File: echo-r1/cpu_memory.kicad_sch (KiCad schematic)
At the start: 48 parts, among them U6 STM32H743IGTx, U7 W9825G6KH-x, Y1 SC-32S32.768kHz20PPM12.5pF, Y2 XTM32024000JT00351001

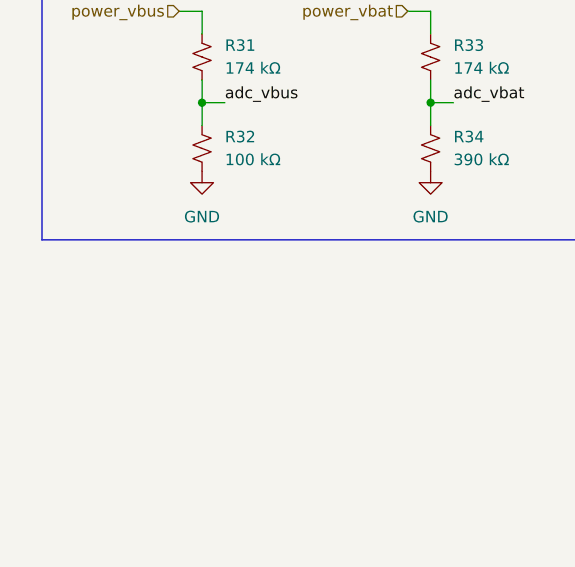
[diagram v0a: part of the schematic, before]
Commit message: R1-Rev1: remove VBUS discharge resistor
This is not needed since there is a path through the ADC
voltage divider to discharge VBUS -- and realistically
the battery charger should also discharge VBUS even with
no resistive path to ground.
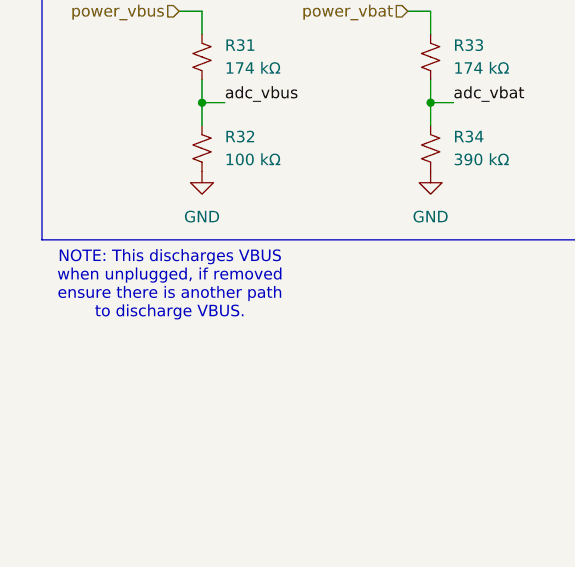
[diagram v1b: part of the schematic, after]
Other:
- note added: "NOTE: This discharges VBUS when unplugged, if removed ensure there is another path to discharge VBUS."
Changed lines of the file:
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@@
+		)
+	)
+	(text "NOTE: This discharges VBUS\nwhen unplugged, if removed\nensure there is another path\nto discharge VBUS."
+		(exclude_from_sim no)
+		(at 29.464 152.4 0)
+		(effects
+			(font
+				(size 1.27 1.27)
+			)
 		)
 	)

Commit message: WIP redesign with STM32H7R3Z8J6
The H7R3 has a bunch of features that greatly simplify the design:
support for HyperRAM, which requires far fewer pins than SDRAM and
is more power efficient; this frees up the FMC to interface with the
display in 8-bit 8080 MCU mode; and there is a built-in USB HS PHY,
removing the need for an external PHY.

The huge reduction in signal count allows for a smaller pin count
package -- only 144 pins. HyperRAM only comes in BGA packages so it
makes sense to also use the UFBGA-144 package for the CPU, which
takes up less than 1/4 of the board area of an LQFP-176 package.
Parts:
- removed C10, C11, C13, C14, C15, C16, C17, C18, C19, C21, C22, C23, C24, C25, C26, C32, C35, C36, C37, C38, C39, C40, C41, C9: 100 nF, Capacitor_SMD:C_0402_1005Metric, symbol Device:C_Small
- removed C12, C20: 1 µF, Capacitor_SMD:C_0402_1005Metric, symbol Device:C_Small
- removed C29: 4.7 µF, Capacitor_SMD:C_0603_1608Metric, symbol Device:C_Small
- removed C33, C34: 2.2 µF, Capacitor_SMD:C_0603_1608Metric, symbol Device:C_Small
- removed R10: 100 kΩ, Resistor_SMD:R_0402_1005Metric, symbol Device:R_Small_US
- removed R11, R12: 10 kΩ, Resistor_SMD:R_0402_1005Metric, symbol Device:R_Small_US
- removed U6: STM32H743IGTx, Package_QFP:LQFP-176_24x24mm_P0.5mm, symbol MCU_ST_STM32H7:STM32H743IGTx
- removed U7: W9825G6KH-x, Package_SO:TSOP-II-54_22.2x10.16mm_P0.8mm, symbol echoplayer:W9825G6KH-5
- added R23, R24: 10 kΩ, Resistor_SMD:R_0603_1608Metric_Pad0.98x0.95mm_HandSolder, symbol Device:R_US
- added U7: STM32H7R3Z8Jx, Package_BGA:UFBGA-144_10x10mm_Layout12x12_P0.8mm, symbol MCU_ST_STM32H7:STM32H7R3Z8Jx
- added U8: W958D8NBYA5I, echoplayer:TFBGA-24_6x8mm_Layout5x5_P1.0mm_Ball0.4mm, symbol echoplayer:W958D8NBYA5I
- renumbered C28 to C10, C30 to C11, C31 to C12, C27 to C9, D12 to D1, D13 to D2, D14 to D3, D15 to D4, R31 to R10, R32 to R11, R33 to R12, R34 to R13
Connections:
- net GND: now also U7.A1 (VSS), U7.A12 (VSS), U7.C9 (VSS), U7.D2 (VSS), U7.D5 (VSS), U7.D7 (VSS), U7.D8 (VSSUSB), U7.E1 (VSSSMPS), U7.E7 (VSS), U7.F5 (VSS), U7.G1 (VSS), U7.G8 (VSS), U7.H3 (VSSA), U7.H4 (VSS), U7.H7 (VSS), U7.K10 (VSS), U7.K6 (VSS), U7.K8 (VSS), U7.M1 (VSS), U7.M12 (VSS), U8.B3 (VSS), U8.C1 (VSSQ), U8.E5 (VSSQ)
- net codec.bclk: now also U7.D1 (PE5)
- net codec.dplay: now also U7.E2 (PE6)
- net codec.drec: now also U7.D3 (PE3)
- net codec.mclk: now also U7.C4 (PE2)
- net codec.wclk: now also U7.E3 (PE4)
- net codec_ctl.scl: now also R24.2, U7.A2 (PB8)
- net codec_ctl.sda: now also R23.2, U7.D4 (PB7)
- net osc24m_in: now also U7.G2 (PH0)
- net osc24m_out: now also U7.H1 (PH1)
- net osc32k_in: now also U7.C1 (PC14)
- net osc32k_out: now also U7.C2 (PC15)
- net power_3v3: now also R23.1, R24.1
- net rtc_wakeup: now also U7.B2 (PC13)
- net sdmmc.clk: now also U7.C12 (PC12)
- net sdmmc.cmd: now also U7.C11 (PD2)
- net sdmmc.d0: now also U7.G11 (PC8)
- net sdmmc.d1: now also U7.G10 (PC9)
- net sdmmc.d2: now also U7.D11 (PC10)
- net sdmmc.d3: now also U7.E9 (PC11)
- net swd_clk: now also U7.E10 (PA14(JTCK)
- net swd_io: now also U7.E12 (PA13(JTMS)
- net swd_nrst: now also U7.F4 (NRST)
- net power_vbus renamed usb_vbus
- net usb_vbus: now also U7.B8 (PM8)
- new net: U8.A5 (RFU), U8.B5 (RFU), U8.C2 (RFU), U8.C5 (RFU)
- new net lcd_mcu.cs: U7.K11 (PD12)
- new net lcd_mcu.d0: U7.E11 (PA12)
- new net lcd_mcu.d1: U7.F12 (PA11)
- new net lcd_mcu.d2: U7.F11 (PA10)
- new net lcd_mcu.d3: U7.G12 (PA9)
- new net lcd_mcu.d4: U7.F10 (PA8)
- new net lcd_mcu.d5: U7.L1 (PA2)
- new net lcd_mcu.d6: U7.J2 (PA1)
- new net lcd_mcu.d7: U7.K1 (PA0)
- new net lcd_mcu.dcx: U7.G5 (PC1)
- new net lcd_mcu.wrx: U7.L5 (PB2)
- new net power_1v8: U7.K5 (VDDXSPI1), U7.K7 (VDDXSPI1), U7.K9 (VDDXSPI1), U8.B4 (VCC), U8.D1 (VCCQ), U8.E4 (VCCQ)
- new net usb_d+: U7.A9 (PM6)
- new net usb_d-: U7.B9 (PM5)
- new net xspi_ck+: U7.M7 (PO4), U8.B2 (CK)
- new net xspi_ck-: U7.L7 (PO5), U8.A2 (CK#)
- new net xspi_cs: U7.J7 (PO0), U8.A3 (CS#)
- new net xspi_d0: U7.L8 (PP0), U8.D3 (DQ0)
- new net xspi_d1: U7.L10 (PP1), U8.D2 (DQ1)
- new net xspi_d2: U7.L6 (PP2), U8.C4 (DQ2)
- new net xspi_d3: U7.M6 (PP3), U8.D4 (DQ3)
- new net xspi_d4: U7.M5 (PP4), U8.D5 (DQ4)
- new net xspi_d5: U7.M8 (PP5), U8.E3 (DQ5)
- new net xspi_d6: U7.M9 (PP6), U8.E2 (DQ6)
- new net xspi_d7: U7.M10 (PP7), U8.E1 (DQ7)
- new net xspi_dqs0: U7.L9 (PO2), U8.C3 (RWDS)
- no-connect marks 8 -> 0
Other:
- note removed: "Any W9825G6KH variant"
- note removed: "BOOT0 must be high to force DFU mode. The STM32H743 has the 'old' ST boot pin structure which requires an external pulldown and cannot be used as a GPIO."
- note removed: "NOTE: As per errata 2.2.28, PC13 toggling can affect the LSE oscillator on LQFP. This is probably not a huge issue if the pin doesn't toggle very frequently, as is the case for RTC wakeup."
- note removed: "Note that the LCD bus connection is MSB to MSB, so in general STM32's LCD_X(n) -> lcd.x(n-2) since the STM32 has an 8 bit per channel LCD controller"
- note removed: "Or STM32H743IIT"
- note removed: "SDRAM"
- note removed: "SDRAM DECOUPLING Place 1x near VDD/VDDQ"
- note removed: "VDD DECOUPLING Place 1x 100 nF near VDD, place 4.7 µF centrally."
- note removed: "VDD33USB DECOUPLING"
- note removed: "VDDA DECOUPLING"
